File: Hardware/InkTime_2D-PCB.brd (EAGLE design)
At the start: 46 x 35 mm, 105 parts, among them IC1 BQ25180YBGR, IC2 DRV2605YZFR, IC3 BMA421, IC9 RT6160AWSC, J1 503480-2400, J2 TC2030-IDC, J4 KH-TYPE-C-16P, Q2 20V/4.2A/52mΩ/1.4W, Q3 SI1308EDL-T1-GE3, U1 NRF52840_QF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

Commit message: Fix antenna cutout and update X2 component library
Fixes #4
Fixes #9
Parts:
- L7: value MLP2016SR47MT0S1_FTC252012SR47MBCA -> FTC252012SR47MBCA
- X2: value 32.768kHz -> 32.768KHz; device adafruit:HC49/S -> InkTime_v5:NORDIC_NRF_1_XTAL_3215_N
- moved ANT1 11.3 mm to (91.7, 63.7), turned to 270 degrees
- moved X2 7.65 mm to (87.0, 73.0), turned to 180 degrees
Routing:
- net GND: track 370.5 -> 363.6 mm
- net N$13: track 12.2 -> 16.5 mm
- net N$8: track 28.2 -> 30.4 mm, vias 1 -> 2
- net N$9: track 21.7 -> 23.4 mm, vias 1 -> 3
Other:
- outline, holes or cut-outs redrawn

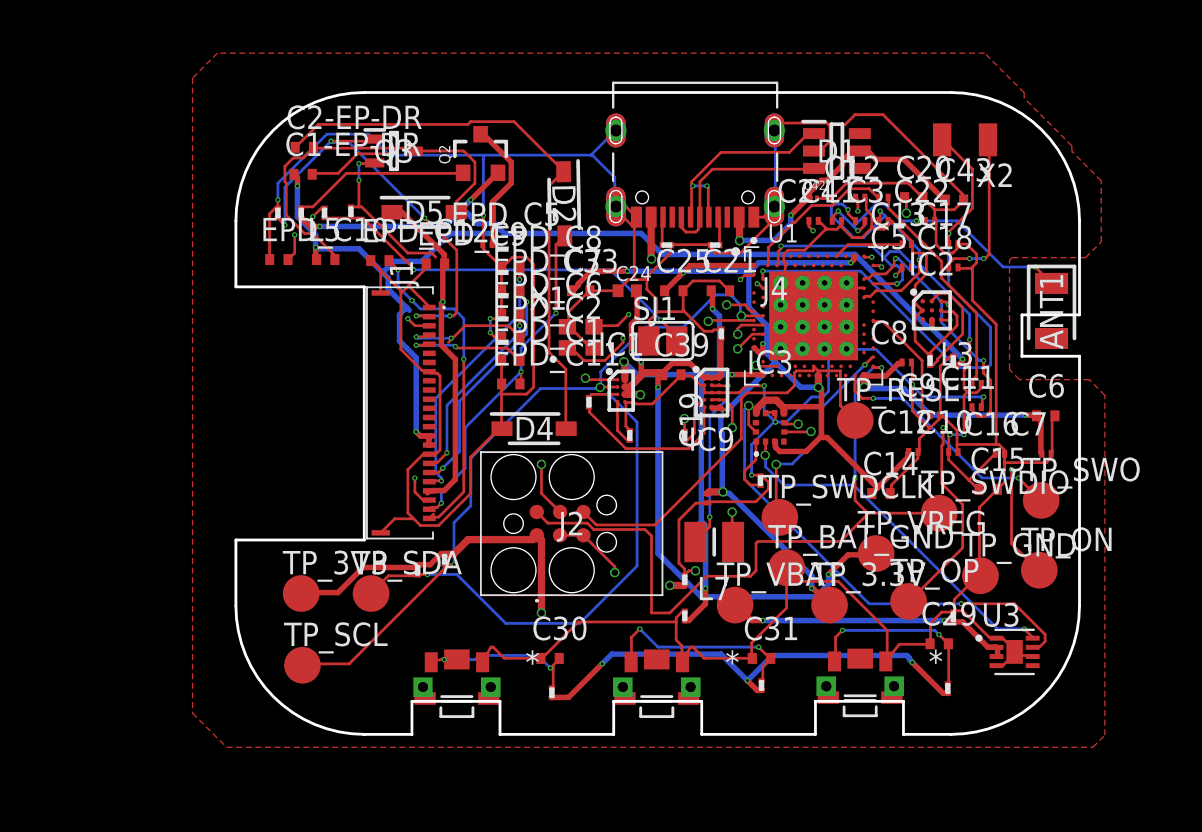
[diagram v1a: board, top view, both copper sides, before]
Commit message: Completed Ground Plane for the 4-layer routing
Fixes #3
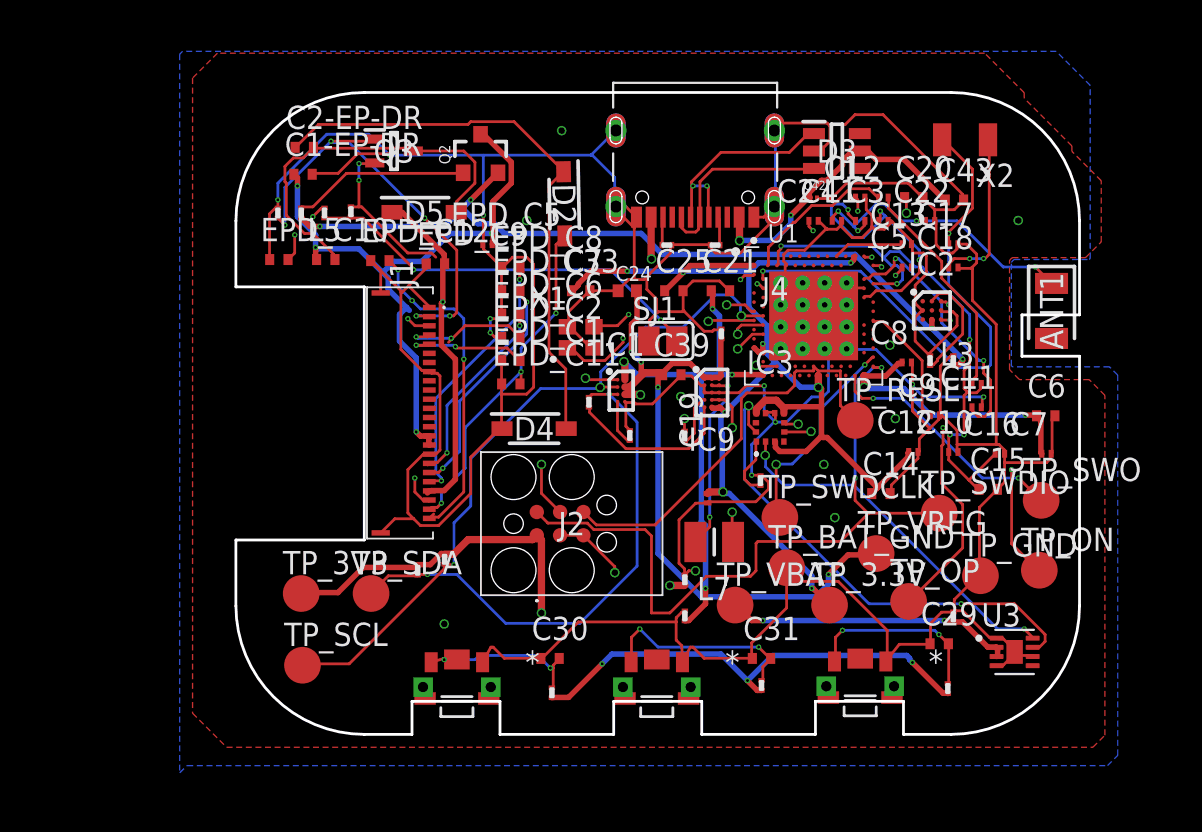
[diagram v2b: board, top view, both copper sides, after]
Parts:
- renumbered D1 to D3
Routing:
- net GND: vias 12 -> 21
- added copper zone on layer 16, net GND
- added copper zone on layer 2, net GND
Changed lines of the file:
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@@
 <attribute name="VALUE" x="83.3504" y="55.98" size="1.27" layer="27"/>
 </element>
-<element uuid="0xABCDEF18" name="D1" library="InkTime_v5" library_urn="urn:adsk.wipprod:fs.file:vf.UGCviqsKRuyr22hNdtfhcA" package="ESP32_C6_LIBRARY_3_SOT95P280X145-6N" value="USBLC6-2SC6Y" x="80.01" y="72.39" smashed="yes">
+<element uuid="0xABCDEF18" name="D3" library="InkTime_v5" library_urn="urn:adsk.wipprod:fs.file:vf.UGCviqsKRuyr22hNdtfhcA" package="ESP32_C6_LIBRARY_3_SOT95P280X145-6N" value="USBLC6-2SC6Y" x="80.01" y="72.39" smashed="yes">
 <attribute name="AVAILABILITY" value="In Stock" x="146.05" y="-90.17" size="1.778" layer="27" display="off"/>
 <attribute name="CHECK_PRICES" value="https://www.snapeda.com/parts/USBLC6-2SC6Y/STMicroelectronics/view-part/?ref=eda" x="146.05" y="-90.17" size="1.778" layer="27" display="off"/>
@@
 <contactref element="J4" pad="A1_B12"/>
 <contactref element="J4" pad="A12_B1"/>
-<contactref element="D1" pad="2"/>
+<contactref element="D3" pad="2"/>
 <contactref element="C42" pad="2"/>
 <contactref element="C43" pad="2"/>
@@
 <wire x1="84.7344" y1="69.7992" x2="84.7024" y2="69.85" width="0.1524" layer="1"/>
 <wire x1="86.5632" y1="67.056" x2="86.5632" y2="67.2846" width="0.1524" layer="1"/>
-<wire x1="86.3346" y1="66.8274" x2="86.5251" y2="67.0179" width="0.1524" layer="1"/>
-<wire x1="86.5251" y1="67.0179" x2="86.5632" y2="67.056" width="0.1524" layer="1"/>
+<wire x1="86.3346" y1="66.8274" x2="86.5632" y2="67.056" width="0.1524" layer="1"/>
 <wire x1="85.8774" y1="66.8274" x2="86.3346" y2="66.8274" width="0.1524" layer="1"/>
 <wire x1="85.4202" y1="67.2846" x2="85.8774" y2="66.8274" width="0.1524" layer="1"/>
@@
 <vertex x="92.8354" y="72.3568375"/>
 </polygon>
+<polygon width="0.1524" layer="16" spacing="1.27" pour="solid" thermals="yes">
+<vertex x="89.6568375" y="66.4646"/>
+<vertex x="89.68484375" y="66.4762"/>
+<vertex x="93.7684375" y="66.4762"/>
+<vertex x="93.8238" y="66.5315625"/>
+<vertex x="93.8238" y="75.9684375"/>
+<vertex x="91.9684375" y="77.8238"/>
+<vertex x="44.3315625" y="77.8238"/>
+<vertex x="44.1762" y="77.6684375"/>
+<vertex x="44.1762" y="38.4839625"/>
+<vertex x="44.5568375" y="38.8646"/>
+<vertex x="44.58484375" y="38.8762"/>
+<vertex x="94.7684375" y="38.8762"/>
+<vertex x="95.3238" y="39.4315625"/>
+<vertex x="95.3238" y="60.1684375"/>
+<vertex x="94.8684375" y="60.6238"/>
+<vertex x="89.58484375" y="60.6238"/>
+<vertex x="89.5568375" y="60.6354"/>
+<vertex x="89.5354" y="60.6568375"/>
+<vertex x="89.5238" y="60.68484375"/>
+<vertex x="89.5238" y="66.31515625"/>
+<vertex x="89.5354" y="66.3431625"/>
+</polygon>
+<polygon width="0.1524" layer="2" spacing="1.27" pour="solid" thermals="yes">
+<vertex x="89.7568375" y="66.3646"/>
+<vertex x="89.78484375" y="66.3762"/>
+<vertex x="93.5684375" y="66.3762"/>
+<vertex x="94.5238" y="67.3315625"/>
+<vertex x="94.5238" y="74.5684375"/>
+<vertex x="91.4684375" y="77.6238"/>
+<vertex x="44.2315625" y="77.6238"/>
+<vertex x="43.1762" y="76.5684375"/>
+<vertex x="43.1762" y="37.3762"/>
+<vertex x="95.0684375" y="37.3762"/>
+<vertex x="95.8238" y="38.1315625"/>
+<vertex x="95.8238" y="59.8684375"/>
+<vertex x="94.8684375" y="60.8238"/>
+<vertex x="89.78484375" y="60.8238"/>
+<vertex x="89.7568375" y="60.8354"/>
+<vertex x="89.7354" y="60.8568375"/>
+<vertex x="89.7238" y="60.88484375"/>
+<vertex x="89.7238" y="66.31515625"/>
+<vertex x="89.7354" y="66.3431625"/>
+</polygon>
+<via x="89.9" y="68.6" extent="1-16" drill="0.35" alwaysstop="yes">
+</via>
+<via x="58.6" y="46.6" extent="1-16" drill="0.35" alwaysstop="yes">
+</via>
+<via x="63.1" y="68.6" extent="1-16" drill="0.35" alwaysstop="yes">
+</via>
+<via x="79.9" y="52.4" extent="1-16" drill="0.35" alwaysstop="yes">
+</via>
+<via x="83.2" y="57.8" extent="1-16" drill="0.35" alwaysstop="yes">
+</via>
+<via x="71.5" y="59" extent="1-16" drill="0.35" alwaysstop="yes">
+</via>
+<via x="65" y="73.5" extent="1-16" drill="0.35" alwaysstop="yes">
+</via>
+<via x="79.3" y="55.3" extent="1-16" drill="0.35" alwaysstop="yes">
+</via>
+<via x="82.9" y="61.8" extent="1-16" drill="0.35" alwaysstop="yes">
+</via>
 </signal>
 <signal name="SWO">
@@
 <contactref element="J4" pad="A6"/>
 <contactref element="J4" pad="B6"/>
-<contactref element="D1" pad="3"/>
+<contactref element="D3" pad="3"/>
 <wire x1="71.5518" y1="68.199" x2="71.5518" y2="68.7324" width="0.1524" layer="1"/>
 <wire x1="71.7804" y1="67.9704" x2="71.5518" y2="68.199" width="0.1524" layer="1"/>
@@
 <contactref element="J4" pad="A7"/>
 <contactref element="J4" pad="B7"/>
-<contactref element="D1" pad="1"/>
+<contactref element="D3" pad="1"/>
 <wire x1="72.0852" y1="70.7136" x2="72.0852" y2="70.485" width="0.1524" layer="1"/>
 <wire x1="72.0852" y1="70.485" x2="72.0852" y2="68.8086" width="0.1524" layer="1"/>
@@
 <contactref element="J4" pad="A4_B9"/>
 <contactref element="J4" pad="A9_B4"/>
-<contactref element="D1" pad="5"/>
+<contactref element="D3" pad="5"/>
 <contactref element="C42" pad="1"/>
 <contactref element="C43" pad="1"/>
@@
 </signal>
 <signal name="D-/1.5D">
-<contactref element="D1" pad="6"/>
+<contactref element="D3" pad="6"/>
 </signal>
 <signal name="D+/1.5D">
-<contactref element="D1" pad="4"/>
+<contactref element="D3" pad="4"/>
 </signal>
 <signal name="OUT+">

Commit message: Placed decoupling capacitors close to the associated pins
Fixes #10
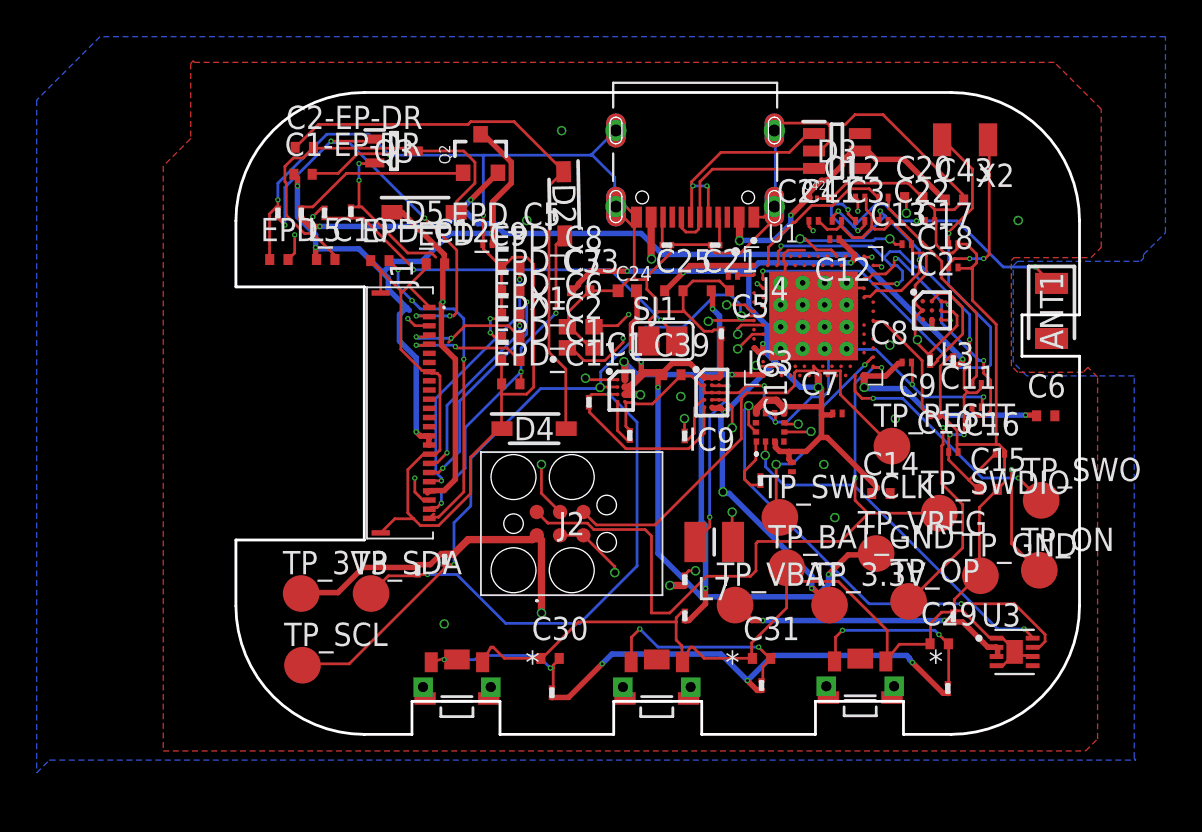
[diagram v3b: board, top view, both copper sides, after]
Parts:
- moved C12 12.4 mm to (79.9, 67.6), turned to 180 degrees
- moved C7 11.6 mm to (80.0, 58.1)
- moved C5 9.49 mm to (74.3, 65.6), turned to 180 degrees
- moved C19 4.90 mm to (77.6, 55.2)
- moved TP_RESET 2.44 mm to (83.0, 56.3)
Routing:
- net GND: track 363.6 -> 335.1 mm
- net N$7: track 10.5 -> 0.98 mm, vias 2 -> 0
- net N$1: track 3.85 -> 13.3 mm, vias 0 -> 2
- net 3V3/2.4A: track 121.2 -> 118.2 mm
- net RESET: track 22.9 -> 25.1 mm

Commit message: Simplified Silkscreen and optimized routing areas
Fixes #11 and Fixes #5
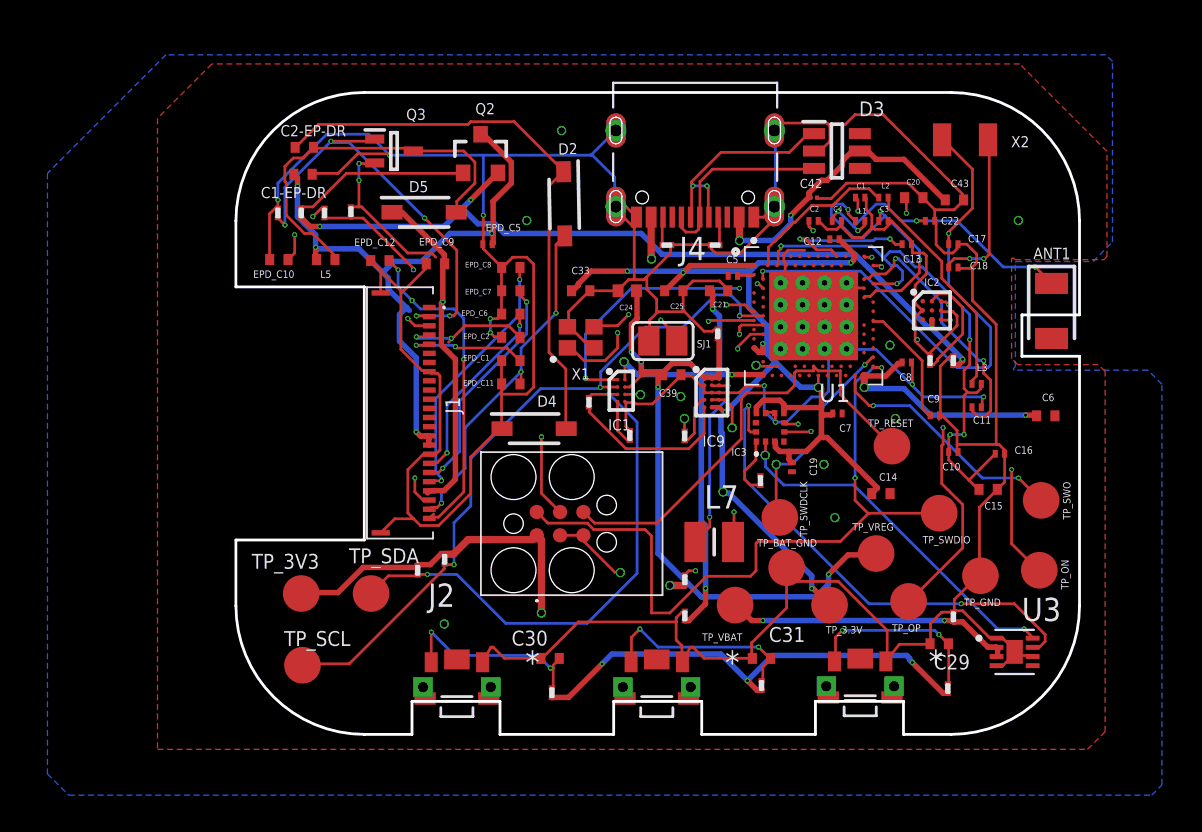
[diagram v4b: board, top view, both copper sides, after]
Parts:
- moved C23 0.20 mm to (73.5, 62.4)
- moved C21 0.10 mm to (73.6, 64.8)
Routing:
- net SWDCLK: track 27.3 -> 30.2 mm
- net P0.13/1.5D: track 8.87 -> 10.9 mm
- net GND: track 335.1 -> 333.3 mm
- net PMIC_INT: track 17.2 -> 19.0 mm, vias 2 -> 3
